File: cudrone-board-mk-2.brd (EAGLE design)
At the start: 100 x 70 mm, 106 parts, among them U1 EDISON_CONNECTOR_FULLMOUNTING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, U10 A2235-H, U11 FTS31XS-U, U2 FTS31XS-U, U4 TPS62065, U5 USD-SOCKETNEW, U6 TXB0108, U8 PCA9306, U9 PCA9306

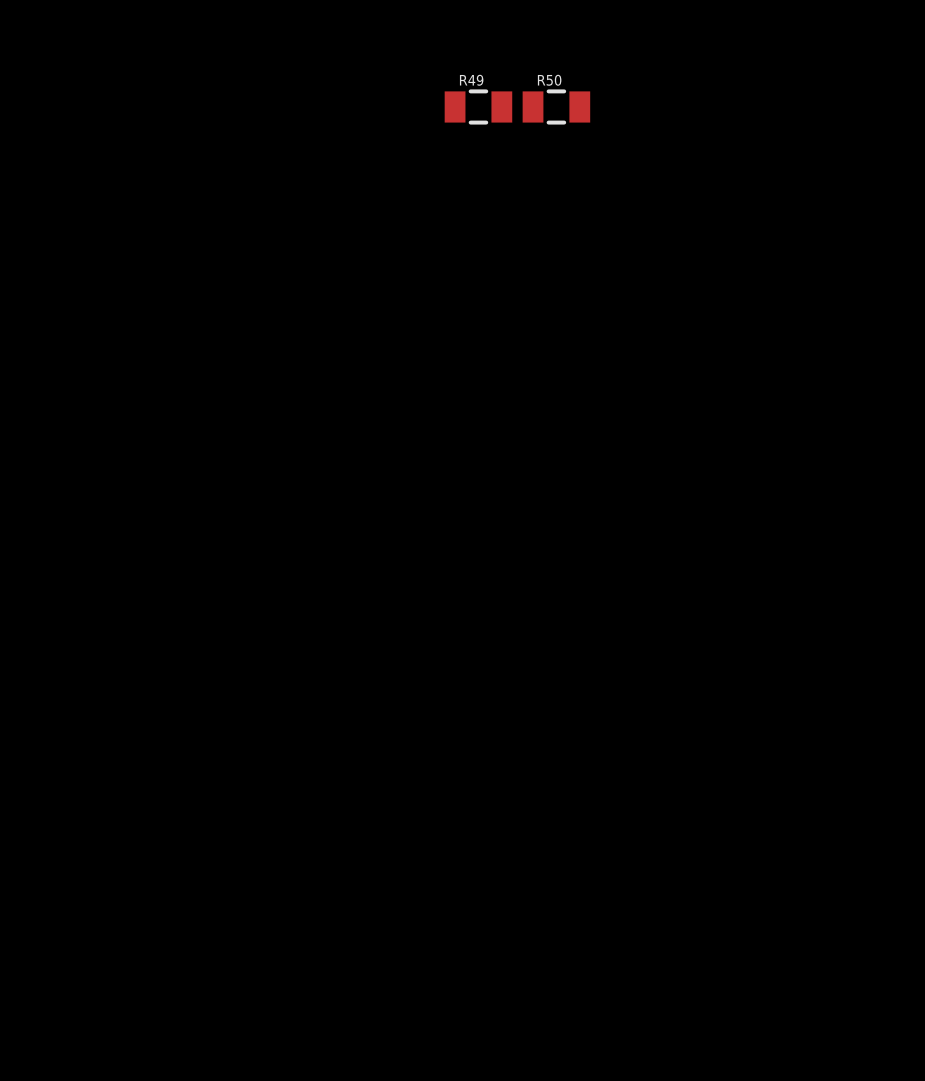
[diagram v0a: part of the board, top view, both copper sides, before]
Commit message: Added flight sensors
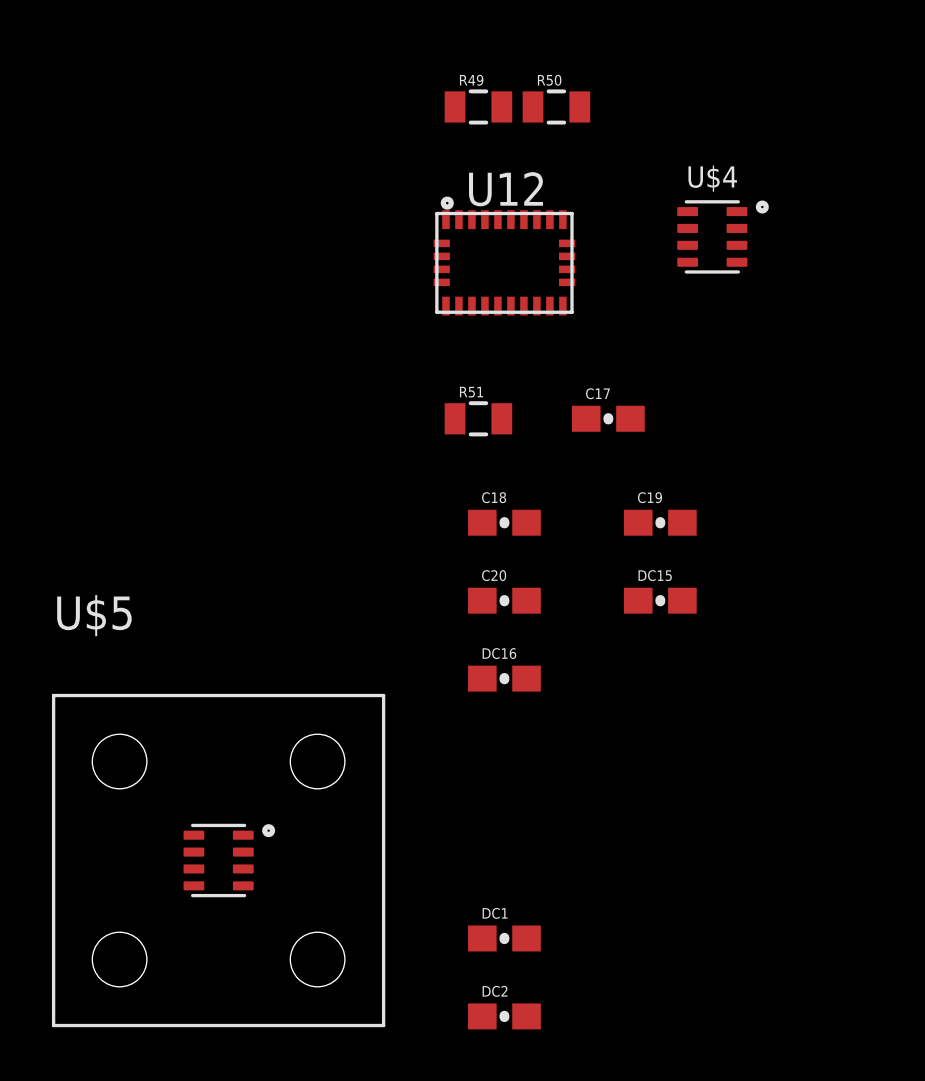
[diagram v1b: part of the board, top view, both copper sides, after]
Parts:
- added C17, C18: 0.1uF, SparkFun-Capacitors:0603-CAP
- added C19: 120nF, SparkFun-Capacitors:0603-CAP
- added C20: 6.8nF, SparkFun-Capacitors:0603-CAP
- added DC1, DC15, DC16, DC2: 100nF, SparkFun-Capacitors:0603-CAP
- added R51: 10k, SparkFun-Resistors:0805
- added U$4: BMP280, BMP280:LGA-8
- added U$5: BMP280PITOT, BMP280:BMP280_PITOT
- added U12: BNO055, BNO055:LGA28R50P4X10_380X520X100
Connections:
- new net I2C0_SCL: U$4.P4, U$5.P4, U12.19
- new net I2C0_SDA: U$4.P3, U$5.P3, U12.20
- new net N$38: C18.1, U12.9
- new net NINT: U12.14
- new net NRESET: R51.2, U12.11
- new net PIN10: U12.10
- net 3.3V: now also C17.1, C19.1, C20.1, DC1.1, DC15.1, DC16.1, DC2.1, R51.1, U$4.P2, U$4.P5, U$4.P6, U$4.P8, U$5.P2, U$5.P5, U$5.P6, U$5.P8, U12.28, U12.3, U12.4
- net GND: now also C17.2, C18.2, C19.2, C20.2, DC1.2, DC15.2, DC16.2, DC2.2, U$4.P1, U$4.P7, U$5.P1, U$5.P7, U12.15, U12.16, U12.17, U12.18, U12.2, U12.25, U12.5, U12.6

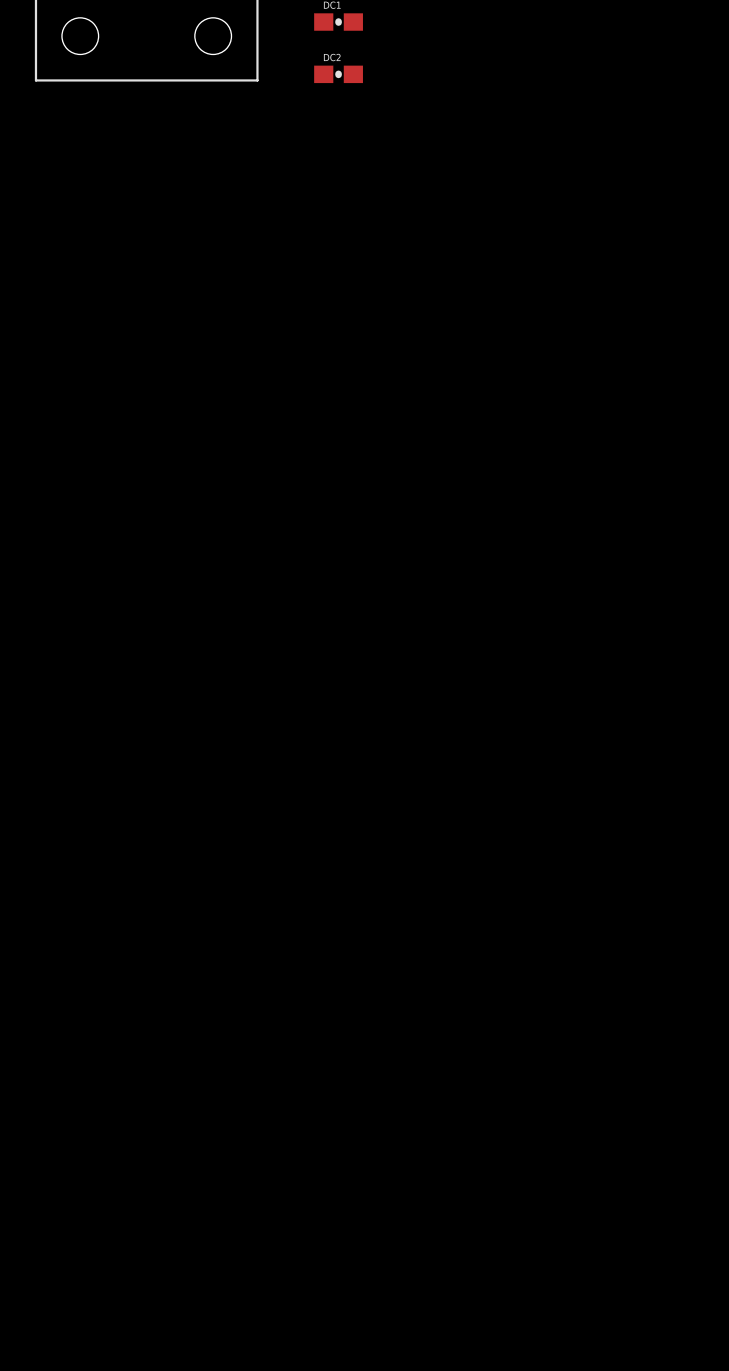
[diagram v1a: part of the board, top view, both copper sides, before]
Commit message: Added xbee and relavent connectors
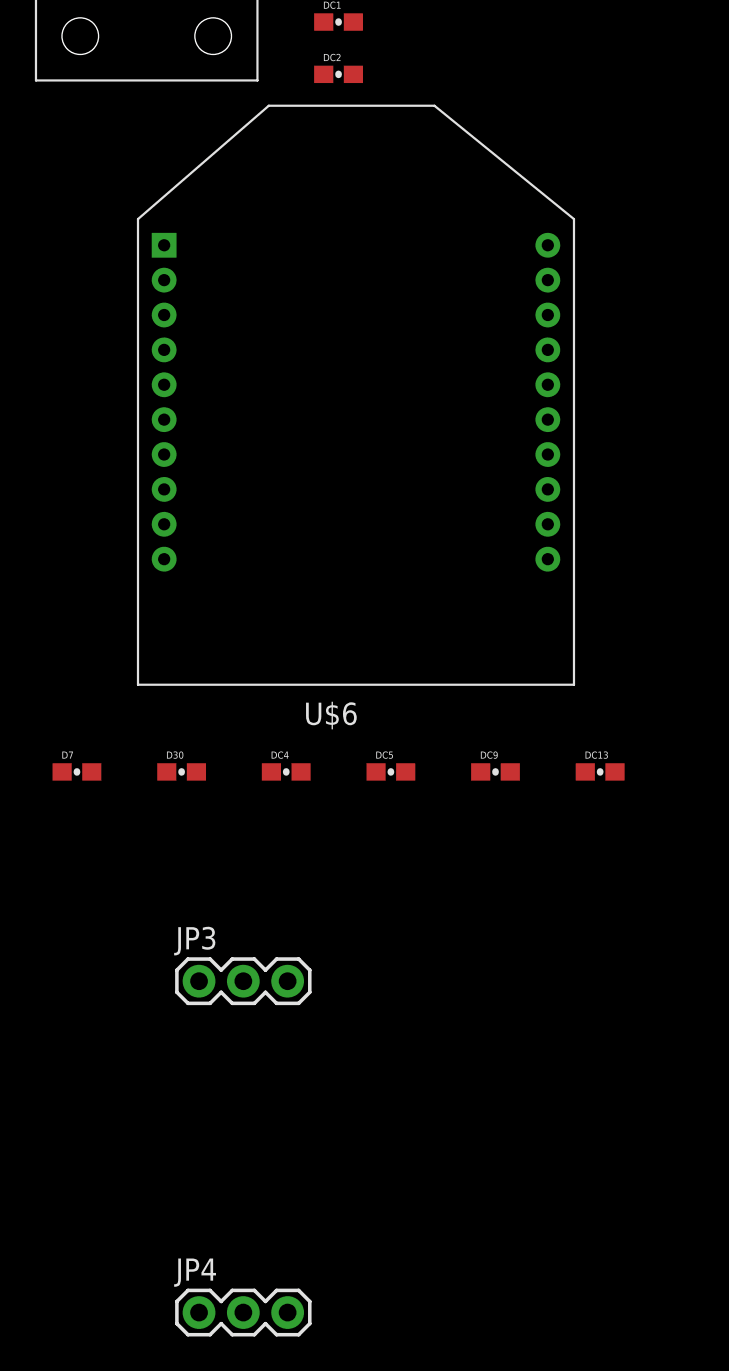
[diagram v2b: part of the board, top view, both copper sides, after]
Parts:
- added D30, D7, DC5, DC9: 10uF, SparkFun-Capacitors:0603-CAP
- added DC13, DC4: 100nF, SparkFun-Capacitors:0603-CAP
- added JP3, JP4: (no value), SparkFun-Connectors:1X03
- added U$6: XBEE, adafruit:XBEE
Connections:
- removed net UART_2_RX: U7.12
- removed net UART_2_TX: U7.13
- new net CON_RX: JP4.1, R7.2
- new net CON_TX: JP3.1, R6.2
- new net CTS_GPIO: U$6.12
- new net RESET: U$6.5
- new net RTS_GPIO: U$6.16
- new net XBEE_RX: U$6.3, U7.13
- new net XBEE_RX_LOW: JP4.3, U7.2
- new net XBEE_TX: U$6.2, U7.12
- new net XBEE_TX_LOW: JP3.3, U7.3
- net 3.3V: now also D30.1, D7.1, DC13.1, DC4.1, DC5.1, DC9.1, U$6.1, U$6.14
- net GND: now also D30.2, D7.2, DC13.2, DC4.2, DC5.2, DC9.2, U$6.10
- net GP134_UART_2_RX: now also JP3.2; no longer R6.2, U7.3
- net GP135_UART_2_TX: now also JP4.2; no longer R7.2, U7.2
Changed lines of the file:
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@@
 <class number="1" name="data" width="0.1524" drill="0">
+</class>
+<class number="2" name="power" width="0.508" drill="0.3048">
+<clearance class="2" value="0.2032"/>
 </class>
 <class number="3" name="power2" width="0.254" drill="0">
@@
 <element name="DC2" library="SparkFun-Capacitors" package="0603-CAP" value="100nF" x="-103" y="-557"/>
 <element name="U$5" library="BMP280" package="BMP280_PITOT" value="BMP280PITOT" x="-114" y="-551"/>
+<element name="U$6" library="adafruit" package="XBEE" value="XBEE" x="-102" y="-585"/>
+<element name="D30" library="SparkFun-Capacitors" package="0603-CAP" value="10uF" x="-112" y="-597"/>
+<element name="DC9" library="SparkFun-Capacitors" package="0603-CAP" value="10uF" x="-94" y="-597"/>
+<element name="DC13" library="SparkFun-Capacitors" package="0603-CAP" value="100nF" x="-88" y="-597"/>
+<element name="DC4" library="SparkFun-Capacitors" package="0603-CAP" value="100nF" x="-106" y="-597"/>
+<element name="DC5" library="SparkFun-Capacitors" package="0603-CAP" value="10uF" x="-100" y="-597"/>
+<element name="D7" library="SparkFun-Capacitors" package="0603-CAP" value="10uF" x="-118" y="-597"/>
+<element name="JP3" library="SparkFun-Connectors" package="1X03" value="" x="-111" y="-609"/>
+<element name="JP4" library="SparkFun-Connectors" package="1X03" value="" x="-111" y="-628"/>
 </elements>
 <signals>
@@
 <contactref element="U$5" pad="P1"/>
 <contactref element="U$5" pad="P7"/>
+<contactref element="U$6" pad="10"/>
+<contactref element="D30" pad="2"/>
+<contactref element="DC9" pad="2"/>
+<contactref element="DC13" pad="2"/>
+<contactref element="D7" pad="2"/>
+<contactref element="DC5" pad="2"/>
+<contactref element="DC4" pad="2"/>
 <wire x1="-91.3175" y1="-412.3203" x2="-90.6825" y2="-417.6797" width="0" layer="19" extent="1-1"/>
 <wire x1="-98.275" y1="-418.3" x2="-90.6825" y2="-417.6797" width="0" layer="19" extent="1-1"/>
@@
 <wire x1="-113.05" y1="-550.025" x2="-102.15" y2="-554" width="0" layer="19" extent="1-1"/>
 <wire x1="-114.95" y1="-550.675" x2="-113.05" y2="-550.025" width="0" layer="19" extent="1-1"/>
+<wire x1="-113" y1="-584.8" x2="-102.15" y2="-557" width="0" layer="19" extent="1-1"/>
+<wire x1="-111.15" y1="-597" x2="-113" y2="-584.8" width="0" layer="19" extent="1-1"/>
+<wire x1="-117.15" y1="-597" x2="-111.15" y2="-597" width="0" layer="19" extent="1-1"/>
+<wire x1="-105.15" y1="-597" x2="-111.15" y2="-597" width="0" layer="19" extent="1-1"/>
+<wire x1="-99.15" y1="-597" x2="-105.15" y2="-597" width="0" layer="19" extent="1-1"/>
+<wire x1="-93.15" y1="-597" x2="-99.15" y2="-597" width="0" layer="19" extent="1-1"/>
+<wire x1="-87.15" y1="-597" x2="-93.15" y2="-597" width="0" layer="19" extent="1-1"/>
 <wire x1="48.37" y1="47.02" x2="-66" y2="-67" width="0" layer="19" extent="1-1"/>
 <wire x1="48.77" y1="47.02" x2="48.37" y2="47.02" width="0" layer="19" extent="1-1"/>
@@
 <contactref element="U$5" pad="P6"/>
 <contactref element="U$5" pad="P5"/>
+<contactref element="U$6" pad="1"/>
+<contactref element="U$6" pad="14"/>
+<contactref element="D30" pad="1"/>
+<contactref element="DC9" pad="1"/>
+<contactref element="DC13" pad="1"/>
+<contactref element="DC4" pad="1"/>
+<contactref element="DC5" pad="1"/>
+<contactref element="D7" pad="1"/>
 <wire x1="-102.15" y1="-402" x2="-102.15" y2="-405" width="0" layer="19" extent="1-1"/>
 <wire x1="-96.15" y1="-402" x2="-102.15" y2="-402" width="0" layer="19" extent="1-1"/>
@@
 <wire x1="-114.95" y1="-551.975" x2="-114.95" y2="-551.325" width="0" layer="19" extent="1-1"/>
 <wire x1="-114.95" y1="-550.025" x2="-114.95" y2="-551.325" width="0" layer="19" extent="1-1"/>
+<wire x1="-113" y1="-566.8" x2="-103.85" y2="-557" width="0" layer="19" extent="1-1"/>
+<wire x1="-91" y1="-578.8" x2="-113" y2="-566.8" width="0" layer="19" extent="1-1"/>
+<wire x1="-88.85" y1="-597" x2="-91" y2="-578.8" width="0" layer="19" extent="1-1"/>
+<wire x1="-94.85" y1="-597" x2="-88.85" y2="-597" width="0" layer="19" extent="1-1"/>
+<wire x1="-100.85" y1="-597" x2="-94.85" y2="-597" width="0" layer="19" extent="1-1"/>
+<wire x1="-106.85" y1="-597" x2="-100.85" y2="-597" width="0" layer="19" extent="1-1"/>
+<wire x1="-112.85" y1="-597" x2="-106.85" y2="-597" width="0" layer="19" extent="1-1"/>
+<wire x1="-118.85" y1="-597" x2="-112.85" y2="-597" width="0" layer="19" extent="1-1"/>
 <wire x1="-73.15" y1="-213" x2="-96.15" y2="-402" width="0" layer="19" extent="1-1"/>
 <wire x1="-65.15" y1="-210" x2="-73.15" y2="-213" width="0" layer="19" extent="1-1"/>
@@
 <signal name="GP135_UART_2_TX">
 <contactref element="U1" pad="27"/>
-<contactref element="R7" pad="2"/>
-<contactref element="U7" pad="2"/>
-<wire x1="-73.54" y1="-188.8" x2="-69.15" y2="-119" width="0" layer="19" extent="1-1"/>
-<wire x1="45.97" y1="47.02" x2="-69.15" y2="-119" width="0" layer="19" extent="1-1"/>
+<contactref element="JP4" pad="2"/>
+<wire x1="45.97" y1="47.02" x2="-108.46" y2="-628" width="0" layer="19" extent="1-1"/>
 </signal>
 <signal name="GP134_UART_2_RX">
 <contactref element="U1" pad="22"/>
-<contactref element="R6" pad="2"/>
-<contactref element="U7" pad="3"/>
-<wire x1="-72.27" y1="-188.8" x2="-73.15" y2="-119" width="0" layer="19" extent="1-1"/>
-<wire x1="47.17" y1="44.38" x2="-73.15" y2="-119" width="0" layer="19" extent="1-1"/>
+<contactref element="JP3" pad="2"/>
+<wire x1="47.17" y1="44.38" x2="-108.46" y2="-609" width="0" layer="19" extent="1-1"/>
 </signal>
 <signal name="GP43_I2S_2_TXD">
@@
 <wire x1="-63.24" y1="-164.3" x2="-72" y2="-178.1" width="0" layer="19" extent="1-1"/>
 </signal>
-<signal name="UART_2_TX">
-<contactref element="U7" pad="13"/>
-</signal>
-<signal name="UART_2_RX">
-<contactref element="U7" pad="12"/>
-</signal>
 <signal name="UART_1_TX">
 <contactref element="U7" pad="11"/>
@@
 <wire x1="-103.75" y1="-529.6625" x2="-103.85" y2="-538" width="0" layer="19" extent="1-1"/>
 </signal>
+<signal name="RESET" class="1">
+<contactref element="U$6" pad="5"/>
+</signal>
+<signal name="XBEE_TX">
+<contactref element="U$6" pad="2"/>
+<contactref element="U7" pad="12"/>
+<wire x1="-72.27" y1="-183.2" x2="-113" y2="-568.8" width="0" layer="19" extent="1-1"/>
+</signal>
+<signal name="XBEE_RX">
+<contactref element="U$6" pad="3"/>
+<contactref element="U7" pad="13"/>
+<wire x1="-73.54" y1="-183.2" x2="-113" y2="-570.8" width="0" layer="19" extent="1-1"/>
+</signal>
+<signal name="RTS_GPIO">
+<contactref element="U$6" pad="16"/>
+</signal>
+<signal name="CTS_GPIO">
+<contactref element="U$6" pad="12"/>
+</signal>
+<signal name="CON_TX">
+<contactref element="R6" pad="2"/>
+<contactref element="JP3" pad="1"/>
+<wire x1="-73.15" y1="-119" x2="-111" y2="-609" width="0" layer="19" extent="1-1"/>
+</signal>
+<signal name="CON_RX">
+<contactref element="R7" pad="2"/>
+<contactref element="JP4" pad="1"/>
+<wire x1="-69.15" y1="-119" x2="-111" y2="-628" width="0" layer="19" extent="1-1"/>
+</signal>
+<signal name="XBEE_TX_LOW">
+<contactref element="U7" pad="3"/>
+<contactref element="JP3" pad="3"/>
+<wire x1="-72.27" y1="-188.8" x2="-105.92" y2="-609" width="0" layer="19" extent="1-1"/>
+</signal>
+<signal name="XBEE_RX_LOW">
+<contactref element="U7" pad="2"/>
+<contactref element="JP4" pad="3"/>
+<wire x1="-73.54" y1="-188.8" x2="-105.92" y2="-628" width="0" layer="19" extent="1-1"/>
+</signal>
 </signals>

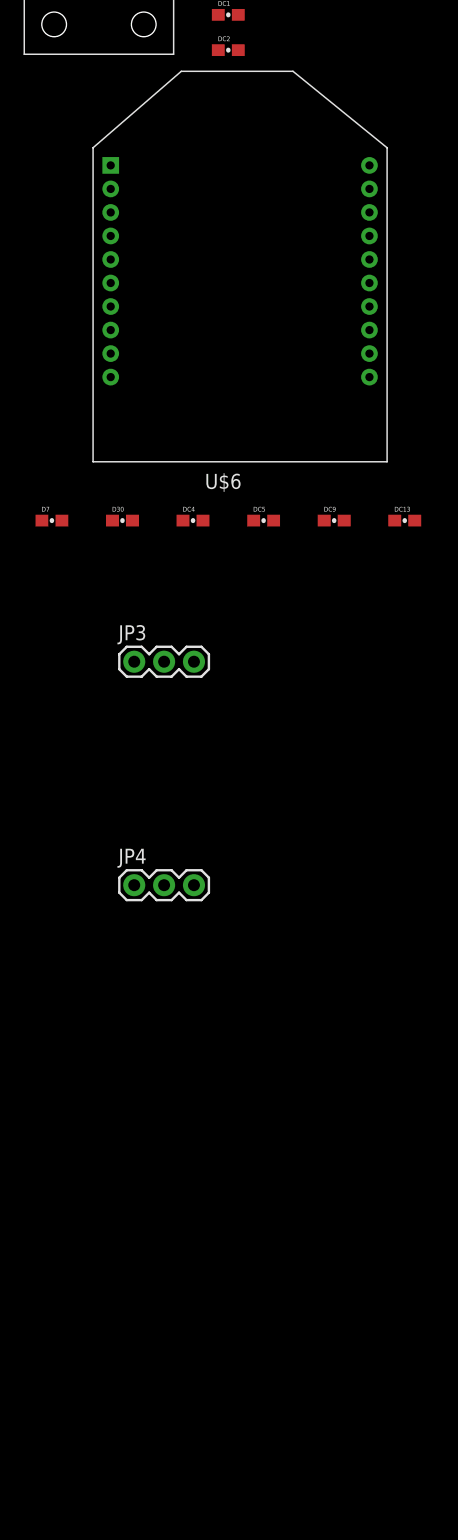
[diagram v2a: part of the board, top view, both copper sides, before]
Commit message: Added GPS and relevent connections
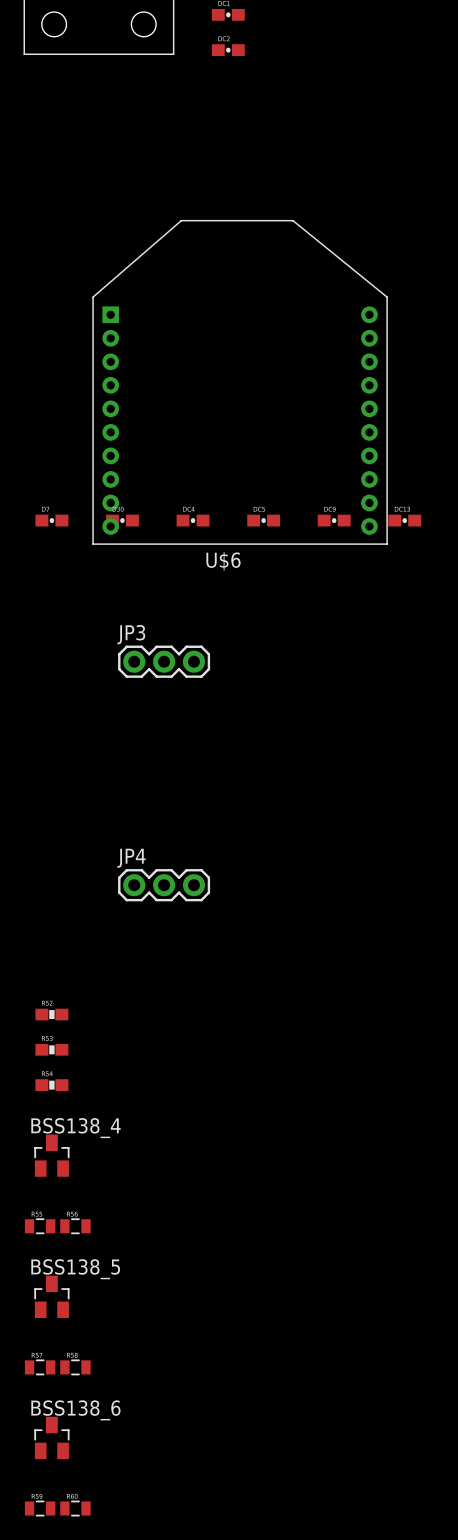
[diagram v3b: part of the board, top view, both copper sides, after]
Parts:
- added BSS138_4, BSS138_5, BSS138_6: PMV22EN, eagle-library-edeca.net-v5:SOT23
- added R52: 10k, SparkFun-Resistors:0603-RES@1
- added R53, R54: 2.2k, SparkFun-Resistors:0603-RES@1
- added R55, R56, R57, R58, R59, R60: 10k, SparkFun-Resistors:0805
- R19, R20, R23, R24: value DNP -> 2.2k
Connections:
- removed net VCC3.3: U10.3
- new net GPS_NRST: BSS138_4.3, R55.2, U10.1
- new net GPS_ON_OFF: BSS138_5.3, R57.2, U10.19
- new net GPS_WAKEUP: BSS138_6.3, R59.2, U10.4
- new net N$39: R52.1, U10.7
- new net N$40: R52.2, U10.5
- new net N$41: R53.1, U10.18
- new net N$42: R54.1, U10.17
- net 1.8V: now also BSS138_4.1, BSS138_5.1, BSS138_6.1, R56.1, R58.1, R60.1
- net 3.3V: now also R53.2, R54.2, R55.1, R57.1, R59.1, U10.3
- net GP165: now also BSS138_6.2, R60.2
- net GP44: now also BSS138_4.2, R56.2
- net GP45: now also BSS138_5.2, R58.2
- net UART_1_TX: now also U10.21, U10.22
